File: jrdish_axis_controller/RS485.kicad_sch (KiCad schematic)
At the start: 46 parts, among them CN3 KF2EDGR-2.54-4P, CN4 KF2EDGR-2.54-4P, CN5 KF2EDGR-2.54-4P, U2 ISOW1432BDFMR, U3 ISOW1432BDFMR

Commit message: Making refinements
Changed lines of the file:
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@@
 	)
 	(symbol
+		(lib_name "KF2EDGR-2.54-4P_1")
 		(lib_id "MyParts:KF2EDGR-2.54-4P")
 		(at 63.5 133.35 0)
@@
 			)
 		)
-		(property "Datasheet" "https://lcsc.com/product-detail/Pluggable-System-Terminal-Block_Cixi-Kefa-Elec-KF2EDGR-2-54-4P_C577596.html"
+		(property "Datasheet" "https://www.lcsc.com/datasheet/C577596.pdf?spm=wm.sxq.inf.ggs&lcsc_vid=FFBaV1wHQFldUVICFgBfBVJTQVJWXgBfEQRYBAFQE1YxVlNRQFRcVVxXQVlZVztW"
 			(at 63.5 147.32 0)
 			(hide yes)
@@
 			)
 		)
-		(property "Description" ""
+		(property "Description" "4 Position Board Side/Socket - Closed 2.54mm Pitch Right-Angle Pin"
 			(at 63.5 133.35 0)
 			(hide yes)
@@
 	)
 	(symbol
+		(lib_name "KF2EDGR-2.54-4P_2")
 		(lib_id "MyParts:KF2EDGR-2.54-4P")
 		(at 63.5 161.29 0)
@@
 			)
 		)
-		(property "Datasheet" "https://lcsc.com/product-detail/Pluggable-System-Terminal-Block_Cixi-Kefa-Elec-KF2EDGR-2-54-4P_C577596.html"
+		(property "Datasheet" "https://www.lcsc.com/datasheet/C577596.pdf?spm=wm.sxq.inf.ggs&lcsc_vid=FFBaV1wHQFldUVICFgBfBVJTQVJWXgBfEQRYBAFQE1YxVlNRQFRcVVxXQVlZVztW"
 			(at 63.5 175.26 0)
 			(hide yes)
@@
 			)
 		)
-		(property "Description" ""
+		(property "Description" "4 Position Board Side/Socket - Closed 2.54mm Pitch Right-Angle Pin"
 			(at 63.5 161.29 0)
 			(hide yes)
@@
 			)
 		)
-		(property "Datasheet" "https://lcsc.com/product-detail/Pluggable-System-Terminal-Block_Cixi-Kefa-Elec-KF2EDGR-2-54-4P_C577596.html"
+		(property "Datasheet" "https://www.lcsc.com/datasheet/C577596.pdf?spm=wm.sxq.inf.ggs&lcsc_vid=FFBaV1wHQFldUVICFgBfBVJTQVJWXgBfEQRYBAFQE1YxVlNRQFRcVVxXQVlZVztW"
 			(at 128.27 185.42 0)
 			(hide yes)
@@
 			)
 		)
-		(property "Description" ""
+		(property "Description" "4 Position Board Side/Socket - Closed 2.54mm Pitch Right-Angle Pin"
 			(at 128.27 171.45 0)
 			(hide yes)

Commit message: Making refinements
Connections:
- net RS485_1_GND: no longer C26.2, C27.2, C28.1, L9.2, U2.13 (MODE)
- net RS485_2_GND: no longer C29.2, C30.2, C31.1, L10.2, U3.13 (MODE)
- removed net GND: C20.1, C21.2, C22.2, C23.1, C24.2, C25.2, C32.1, C33.2, C34.2, C35.1, C36.2, C37.2, U2.10 (GND1), U2.6 (GNDIO), U3.10 (GND1), U3.6 (GNDIO)
- new net: C26.2, C27.2, C28.1, U2.13 (MODE)
- new net: C29.2, C30.2, C31.1, U3.13 (MODE)
- new net: C20.1, C21.2, C22.2, U2.6 (GNDIO)
- new net: C23.1, C24.2, C25.2, U3.6 (GNDIO)
- new net: C32.1, C33.2, C34.2, U2.10 (GND1)
- new net: C35.1, C36.2, C37.2, U3.10 (GND1)
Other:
- note added: "Pins 7 and 14 are left unconnected, not needed"
- title: (none) -> RS485
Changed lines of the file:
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@@
 	(paper "A4")
 	(title_block
-		(date "2026-04-12")
+		(title "RS485")
+		(date "2026-04-30")
 		(rev "1.0")
 		(company "JRSeti")
@@
 		)
 	)
+	(text "Pins 7 and 14 are left unconnected, not needed"
+		(exclude_from_sim no)
+		(at 207.772 34.798 0)
+		(effects
+			(font
+				(size 1.27 1.27)
+			)
+		)
+	)
 	(text "Caps near VIO"
 		(exclude_from_sim no)
@@
 		)
 	)
+	(text "Pins 7 and 14 are left unconnected, not needed"
+		(exclude_from_sim no)
+		(at 70.612 35.306 0)
+		(effects
+			(font
+				(size 1.27 1.27)
+			)
+		)
+	)
 	(text "RS485_1_TX"
 		(exclude_from_sim no)
@@
 	)
 	(symbol
+		(lib_name "BLM15EX331SN1D_3")
 		(lib_id "MyParts:BLM15EX331SN1D")
 		(at 171.45 66.04 0)
@@
 	)
 	(symbol
+		(lib_name "BLM15EX331SN1D_4")
 		(lib_id "MyParts:BLM15EX331SN1D")
 		(at 35.56 66.04 0)
@@
 			)
 		)
-		(property "Datasheet" "https://www.lcsc.com/datasheet/C5216543.pdf"
+		(property "Datasheet" "https://www.ti.com/lit/ds/symlink/isow1432.pdf?ts=1648465263803&ref_url=https%253A%252F%252Fwww.google.com%252F"
 			(at 86.36 78.74 0)
 			(hide yes)
@@
 			)
 		)
-		(property "Datasheet" "https://www.lcsc.com/datasheet/C5216543.pdf"
+		(property "Datasheet" "https://www.ti.com/lit/ds/symlink/isow1432.pdf?ts=1648465263803&ref_url=https%253A%252F%252Fwww.google.com%252F"
 			(at 222.25 78.74 0)
 			(hide yes)

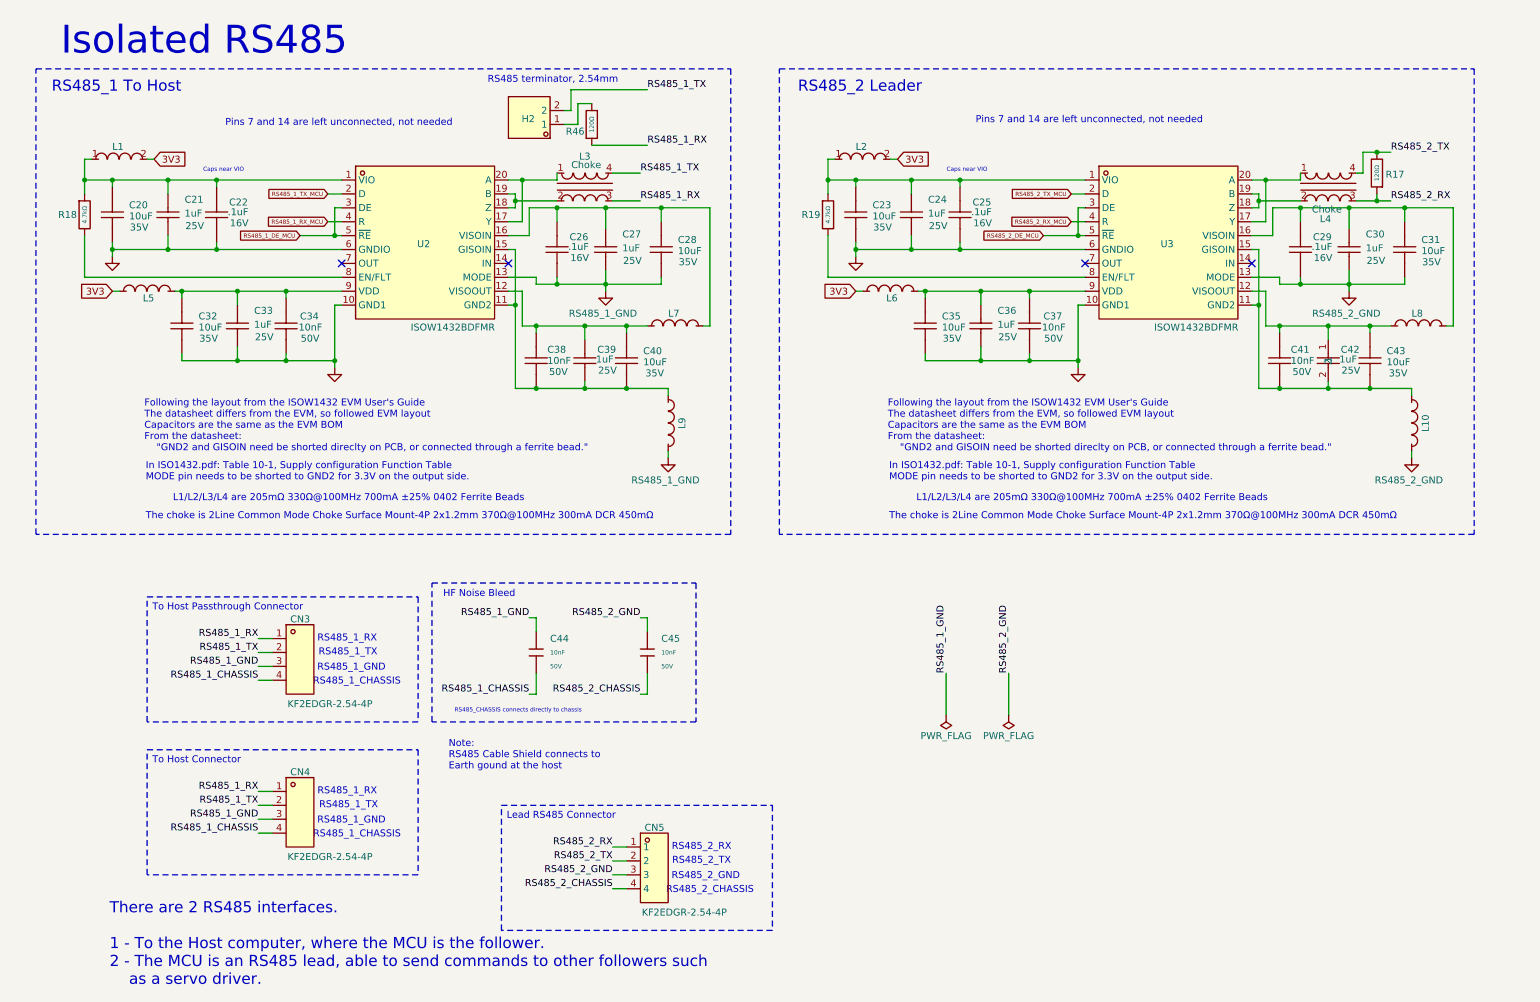
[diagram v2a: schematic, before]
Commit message: Limit switches with mosfets
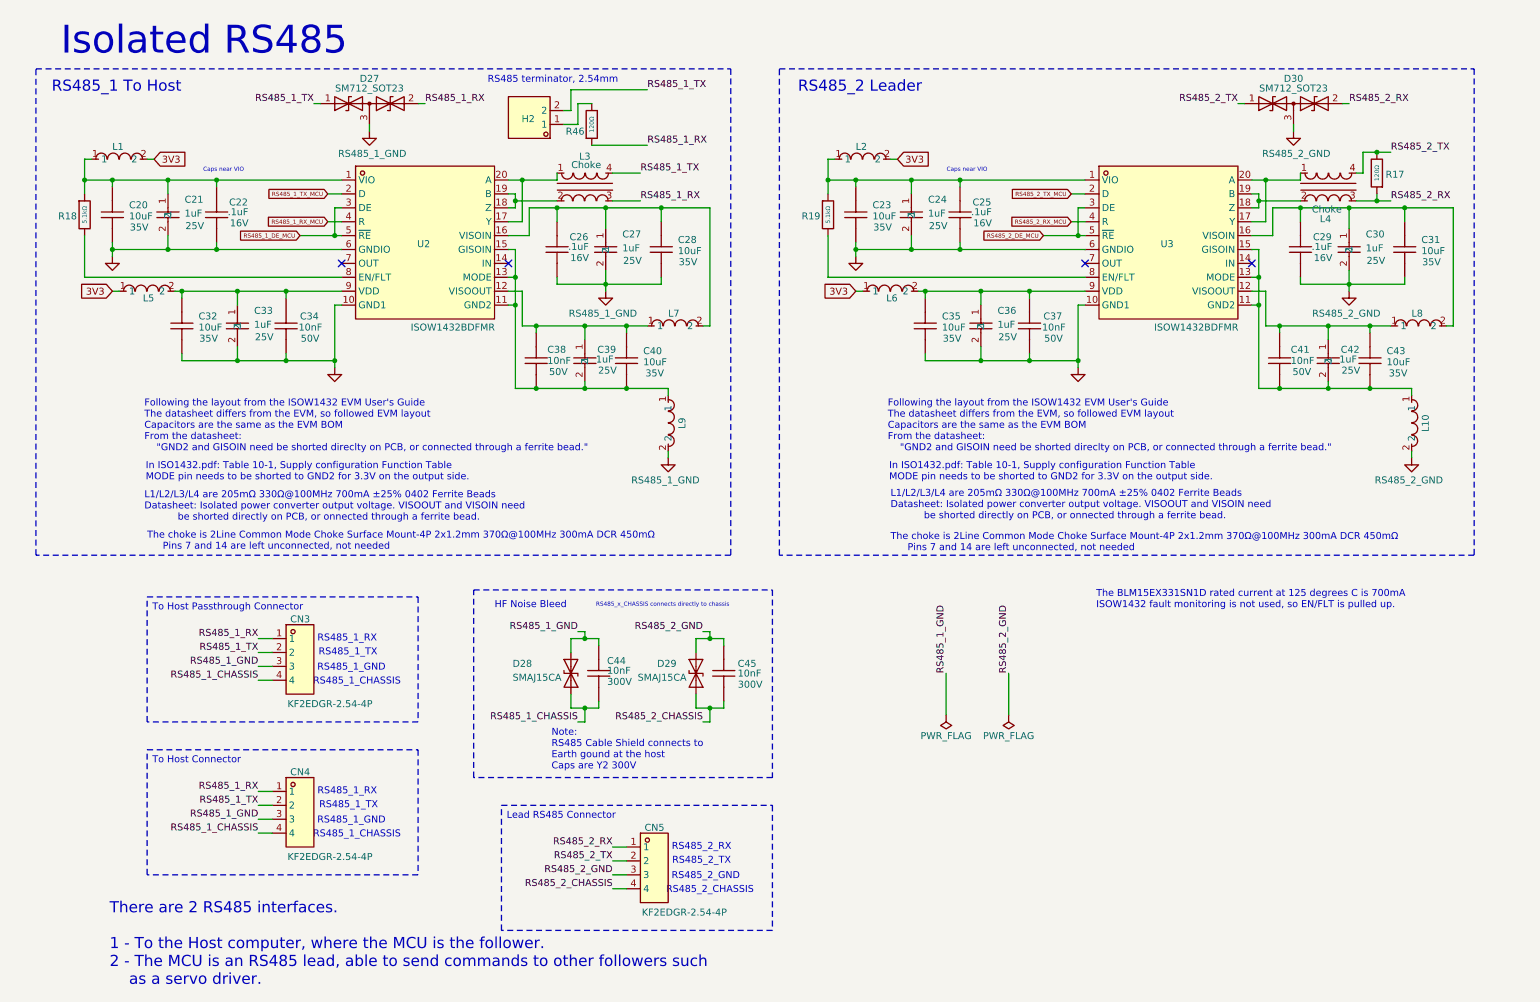
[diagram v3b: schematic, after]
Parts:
- removed C44, C45: 10nF, PCM_JLCPCB:C_0402, symbol PCM_JLCPCB-Capacitors:0402,10nF
- removed R18, R19: 4.7kΩ, PCM_JLCPCB:R_0402, symbol PCM_JLCPCB-Resistors:0402,4.7kΩ
- added C44, C45: 10nF, MyParts:CAP-TH_L13.0-W6.0-P10.00-D1.2, symbol MyParts:C43Q1103K40C80F
- added D27, D30: SM712_SOT23, Package_TO_SOT_SMD:SOT-23, symbol Diode:SM712_SOT23
- added D28, D29: SMAJ15CA, Diode_SMD:D_SMA, symbol Diode:SMAJ15CA
- added R18, R19: 5.1kΩ, PCM_JLCPCB:R_0402, symbol PCM_JLCPCB-Resistors:0402,5.1kΩ
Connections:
- net RS485_1_CHASSIS: now also C44.2, D28.1 (A1)
- net RS485_1_GND: now also C26.2, C27.2, C28.1, L9.2, C44.1, D27.3 (common), D28.2 (A2)
- net RS485_1_RX: now also D27.2 (A2)
- net RS485_1_TX: now also D27.1 (A1)
- net RS485_2_CHASSIS: now also C45.2, D29.1 (A1)
- net RS485_2_GND: now also C29.2, C30.2, C31.1, L10.2, C45.1, D29.2 (A2), D30.3 (common)
- net RS485_2_RX: now also D30.2 (A2)
- net RS485_2_TX: now also D30.1 (A1)
- net at C23.2, C24.1, C25.1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: now also R19.1
- net at U3.8 (EN/FLT): now also R19.2
- net at C41.2, C42.2, C43.1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: now also U3.13 (MODE)
- net at C38.2, C39.2, C40.1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: now also U2.13 (MODE)
- net GND: now reaches C20.1, C21.2, C22.2, U2.6 (GNDIO)
- net GND: now also C23.1, C24.2, C25.2, C32.1, C33.2, C34.2, C35.1, C36.2, C37.2, U2.10 (GND1), U3.10 (GND1), U3.6 (GNDIO)
- net at C20.2, C21.1, C22.1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: now also R18.1
- net at U2.8 (EN/FLT): now also R18.2
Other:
- note added: "L1/L2/L3/L4 are 205mΩ 330Ω@100MHz 700mA ±25% 0402 Ferrite Beads Datasheet: Isolated power converter output voltage. VISOOUT and VISOIN need be shorted directly on PCB, or onnected through a ferrite bead."
- note added: "Note: RS485 Cable Shield connects to Earth gound at the host Caps are Y2 300V"
- note added: "RS485_x_CHASSIS connects directly to chassis"
- note added: "The BLM15EX331SN1D rated current at 125 degrees C is 700mA ISOW1432 fault monitoring is not used, so EN/FLT is pulled up."
- note removed: "L1/L2/L3/L4 are 205mΩ 330Ω@100MHz 700mA ±25% 0402 Ferrite Beads"
- note removed: "Note: RS485 Cable Shield connects to Earth gound at the host"
- note removed: "RS485_CHASSIS connects directly to chassis"

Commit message: Refinements...
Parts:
- C22, C25, C26, C29: value .1uF -> 100nF
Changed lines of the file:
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@@
 	(text "RS485_2_GND"
 		(exclude_from_sim no)
-		(at 137.668 172.974 0)
+		(at 137.6741 172.974 0)
 		(effects
 			(font
@@
 	(text "RS485_2_TX"
 		(exclude_from_sim no)
-		(at 136.906 170.18 0)
+		(at 136.8274 170.18 0)
 		(effects
 			(font
@@
 	(text "RS485_1_RX"
 		(exclude_from_sim no)
-		(at 72.136 157.48 0)
+		(at 72.2086 157.48 0)
 		(effects
 			(font
@@
 	(text "RS485_2_RX"
 		(exclude_from_sim no)
-		(at 136.906 167.64 0)
+		(at 136.9786 167.64 0)
 		(effects
 			(font
@@
 	(text "RS485_2_CHASSIS"
 		(exclude_from_sim no)
-		(at 138.43 175.514 0)
+		(at 139.7 175.514 0)
 		(effects
 			(font
@@
 	(text "RS485_1_GND"
 		(exclude_from_sim no)
-		(at 72.898 162.814 0)
+		(at 72.9041 162.814 0)
 		(effects
 			(font
@@
 	(text "RS485_1_CHASSIS"
 		(exclude_from_sim no)
-		(at 73.914 165.354 0)
+		(at 74.93 165.354 0)
 		(effects
 			(font
@@
 	(text "RS485_1_TX"
 		(exclude_from_sim no)
-		(at 72.39 160.02 0)
+		(at 72.0574 160.274 0)
 		(effects
 			(font
@@
 			)
 		)
-		(property "Value" ".1uF"
+		(property "Value" "100nF"
 			(at 112.522 57.912 90)
 			(show_name no)
@@
 			)
 		)
-		(property "Value" ".1uF"
+		(property "Value" "100nF"
 			(at 50.292 51.562 90)
 			(show_name no)
@@
 			)
 		)
-		(property "Value" ".1uF"
+		(property "Value" "100nF"
 			(at 186.182 51.562 90)
 			(show_name no)
@@
 			)
 		)
-		(property "Value" ".1uF"
+		(property "Value" "100nF"
 			(at 248.412 57.912 90)
 			(show_name no)

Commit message: Minor adjustments
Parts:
- D27, D30: LCSC (none) -> C172881
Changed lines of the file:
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@@
+			)
+		)
+		(property "LCSC" "C172881"
+			(at 245.11 31.75 0)
+			(hide yes)
+			(show_name no)
+			(do_not_autoplace no)
+			(effects
+				(font
+					(size 1.27 1.27)
+				)
 			)
 		)
@@
 			(at 76.2 31.75 0)
 			(hide yes)
+			(show_name no)
+			(do_not_autoplace no)
+			(effects
+				(font
+					(size 1.27 1.27)
+				)
+			)
+		)
+		(property "LCSC" "C172881"
+			(at 76.2 31.75 0)
+			(hide yes)
